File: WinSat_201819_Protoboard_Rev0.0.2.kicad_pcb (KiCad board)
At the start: 4 copper layers, 35.5 x 57.5 mm, 73 parts, among them J1 Conn_01x02_Female, J10 Conn_01x06_Male, J2 Conn_01x02_Female, J3 Conn_01x02_Female, J4 Conn_01x02_Female, J5 Conn_01x03_Female, J6 Conn_01x02_Female, J7 JTAG-6PIN, J8 Conn_01x03_Female, J9 Conn_01x03_Female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

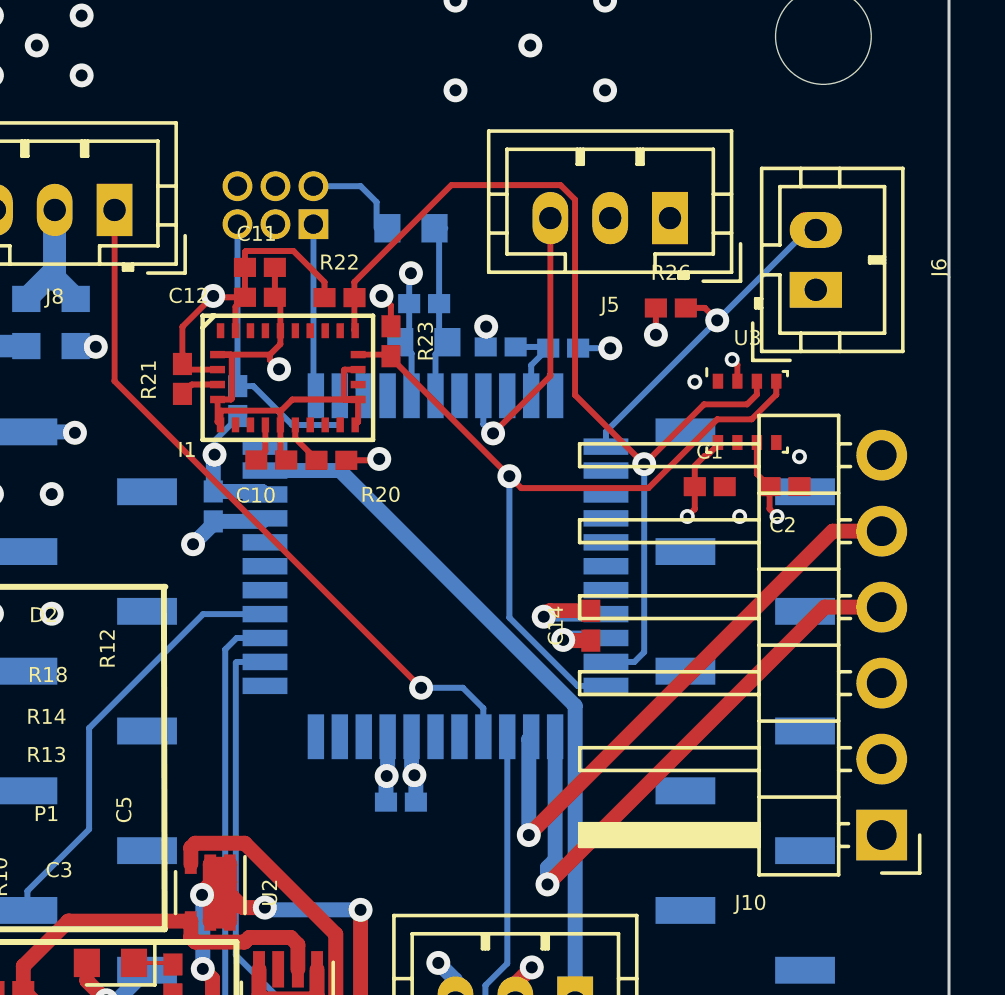
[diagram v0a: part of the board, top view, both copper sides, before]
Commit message: Cleaned up a few traces, fixed shoddy decoupling
Also moved BMP180 away from openlog header
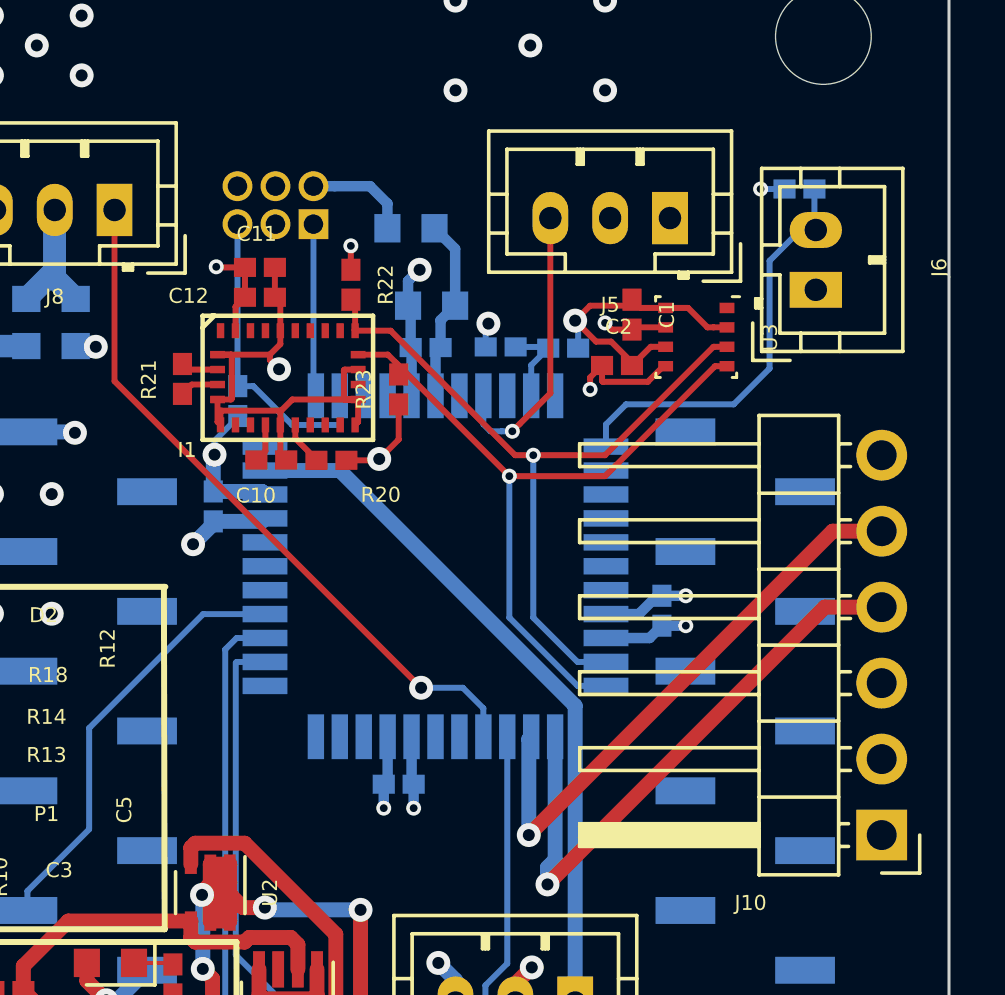
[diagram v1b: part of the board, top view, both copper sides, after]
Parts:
- C14, R26: moved to B.Cu
- moved C2 6.91 mm to (88.4, 85.7), turned to 180 degrees
- moved C1 6.31 mm to (88.9, 84.0), turned to 270 degrees
- moved R26 5.86 mm to (94.5, 79.8)
- moved U3 3.02 mm to (91.0, 84.8), turned to 270 degrees
- moved C14 2.43 mm to (89.9, 93.9)
- moved R23 1.63 mm to (81.1, 86.5), turned to 90 degrees
- moved C9 1.47 mm to (82.0, 85.1)
- moved C8 1.25 mm to (82.2, 83.7)
- moved C13 0.60 mm to (81.1, 99.7)
- moved R22 0.57 mm to (79.5, 83.0), turned to 270 degrees
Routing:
- net SDA1: track 33.2 -> 25.3 mm
- net GND: track 84.6 -> 90.1 mm, vias 39 -> 38
- net TEMP_SENSE-ADC: track 12.2 -> 14.0 mm, vias 1 -> 0
- net SCL1: track 26.5 -> 24.9 mm
- net +3V3: track 61.8 -> 60.6 mm, vias 21 -> 18

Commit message: Proto Final?
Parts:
- removed R17, R27: 1M, Resistor_SMD:R_0805_2012Metric
- added D4: DIODE, Diode_SMD:D_0603_1608Metric, B.Cu at (86.6, 120.9)
- added J11: USB_B_Micro, Connector_USB:USB_Micro-B_Molex-105017-0001, B.Cu at (86.4, 124.5)
- moved MK1 27.5 mm to (95.5, 124.0)
- moved MK3 27.4 mm to (68.1, 124.0)
- moved MK2 0.21 mm to (95.5, 74.7)
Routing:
- net +3V3: track 60.6 -> 51.9 mm
- net Net-(D4-Pad1): track 0.00 -> 2.21 mm
- net GND: track 90.1 -> 91.4 mm, vias 38 -> 63
- net BAT_POS: track 77.8 -> 78.7 mm, vias 2 -> 3
- net Net-(C8-Pad1): vias 0 -> 1
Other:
- board text added: "FTDI/ OPENLOG"
- board text added: "GPS"
- board text added: "HALL"
- board text added: "MOS0"
- board text added: "MOS1"
- board text added: "MOS2"
- board text added: "PDI"
- board text added: "SERVO"
- board text added: "THERM"

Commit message: Fixed Issues Thomas Saw
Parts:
- removed R18: 100k, OSD335x-KiCad-master:Not_Broken_0402
- added C16: 100nF, OSD335x-KiCad-master:Not_Broken_0402, F.Cu at (73.7, 84.6)
- J4: footprint Connector_PinHeader_2.54mm:PinHeader_1x02_P2.54mm_Vertical -> Connector_JST:JST_PH_B2B-PH-K_1x02_P2.00mm_Vertical
- R25: value 66K -> 7.15K
- moved R24 17.1 mm to (69.6, 86.6), turned to 180 degrees
- moved R25 13.3 mm to (71.4, 87.4), turned to 90 degrees
- moved R12 2.58 mm to (71.6, 108.0), turned to 0 degrees
- moved Q4 2.37 mm to (77.7, 122.9)
- moved D3 1.94 mm to (80.3, 123.4), turned to 270 degrees
- moved J4 1.94 mm to (73.7, 118.9), turned to 270 degrees
- moved D2 1.01 mm to (72.1, 106.4), turned to 0 degrees
- moved R21 0.50 mm to (73.7, 86.6)
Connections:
- R24 pad 2: +3V3 -> BAT_POS
- U9 pad 15: SERVO_TCL -> Net-(U9-Pad15)
- U9 pad 16: Net-(U9-Pad16) -> GPS_TX-MCU_RX
- U9 pad 29: Net-(U9-Pad29) -> SERVO_TCL
- U9 pad 32: GPS_TX-MCU_RX -> Net-(U9-Pad32)
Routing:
- net VOLTDIV_ADC: track 2.93 -> 19.3 mm, vias 0 -> 2
- net GPS_TX-MCU_RX: track 23.5 -> 10.6 mm, vias 0 -> 1
- net SERVO_TCL: track 23.5 -> 14.0 mm
- net GND: track 91.4 -> 99.6 mm, vias 63 -> 69
- net Net-(P1-Pad7): track 4.05 -> 0.00 mm
- net Net-(J4-Pad1): track 1.84 -> 4.38 mm
- net FTDI_OLOG_TX-MCU_RX: track 20.1 -> 17.6 mm
- net +3V3: track 51.9 -> 53.6 mm, vias 18 -> 19
- net FTDI_OLOG_RX-MCU_TX: track 19.3 -> 18.0 mm
- net REG_OUT: track 14.6 -> 13.4 mm
- net Net-(D3-Pad1): track 2.74 -> 3.43 mm
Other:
- board text added: "POW"

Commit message: Not sure what updated.
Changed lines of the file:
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@@
     (tags resistor)
     (attr smd)
-    (fp_text reference R12 (at -10.6194 2.6332) (layer F.SilkS)
+    (fp_text reference R12 (at -2.286 -11.43) (layer F.SilkS)
       (effects (font (size 0.5 0.5) (thickness 0.08)))
     )
@@
     (tags diode)
     (attr smd)
-    (fp_text reference D2 (at 2.0697 10.7298) (layer F.SilkS)
-      (effects (font (size 0.5 0.5) (thickness 0.08)))
-    )
+    (fp_text reference D2 (at -2.286 -10.922) (layer F.SilkS)
+      (effects (font (size 0.5 0.5) (thickness 0.08)))
+    )

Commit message: Change Board Size
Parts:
- added MK4: Mounting_Hole, MountingHole:MountingHole_3.2mm_M3, F.Cu at (57.2, 73.4)
- R29: value 0.025 OHM -> 0.05 OHM
- moved MK3 10.9 mm to (57.2, 124.3)
- moved MK2 1.34 mm to (95.3, 73.4)
- moved MK1 0.36 mm to (95.2, 124.2)
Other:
- board size 35.5 x 57.5 mm -> 46.7 x 59.5 mm
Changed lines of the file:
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@@
   (general
     (thickness 1.6)
-    (drawings 23)
+    (drawings 27)
     (tracks 616)
     (zones 0)
-    (modules 73)
+    (modules 74)
     (nets 102)
   )
@@
   (layers
     (0 F.Cu mixed)
-    (1 In1.Cu power)
-    (2 In2.Cu power)
+    (1 In1.Cu power hide)
+    (2 In2.Cu power hide)
     (31 B.Cu jumper)
     (36 B.SilkS user)
     (37 F.SilkS user)
-    (38 B.Mask user)
+    (38 B.Mask user hide)
     (39 F.Mask user)
     (44 Edge.Cuts user)
-    (45 Margin user)
+    (45 Margin user hide)
     (46 B.CrtYd user)
     (47 F.CrtYd user)
@@
     (add_net XBEE_TX-MCU_RX)
   )
+  (module MountingHole:MountingHole_3.2mm_M3 (layer F.Cu)
+    (at 57.2262 73.406)
+    (descr "Mounting Hole 3.2mm, no annular, M3")
+    (tags "mounting hole 3.2mm no annular m3")
+    (attr virtual)
+    (fp_text reference MK4 (at 0 -4.2) (layer F.SilkS) hide
+      (effects (font (size 1 1) (thickness 0.15)))
+    )
+    (fp_text value Mounting_Hole (at 0 4.2) (layer F.Fab)
+      (effects (font (size 1 1) (thickness 0.15)))
+    )
+    (fp_text user %R (at 0.3 0) (layer F.Fab)
+      (effects (font (size 1 1) (thickness 0.15)))
+    )
+    (fp_circle (center 0 0) (end 3.2 0) (layer Cmts.User) (width 0.15))
+    (fp_circle (center 0 0) (end 3.45 0) (layer F.CrtYd) (width 0.05))
+    (pad 1 np_thru_hole circle (at 0 0) (size 3.2 3.2) (drill 3.2) (layers *.Cu *.Mask))
+  )
   (module OSD335x-KiCad-master:Not_Broken_0402 (layer F.Cu)
     (at 73.66 84.582 270)
@@
   )
   (module MountingHole:MountingHole_3.2mm_M3 (layer F.Cu)
-    (at 95.504 123.952)
+    (at 95.25 124.206)
     (descr "Mounting Hole 3.2mm, no annular, M3")
     (tags "mounting hole 3.2mm no annular m3")
@@
   )
   (module MountingHole:MountingHole_3.2mm_M3 (layer F.Cu)
-    (at 95.504 74.676)
+    (at 95.3008 73.3552)
     (descr "Mounting Hole 3.2mm, no annular, M3")
     (tags "mounting hole 3.2mm no annular m3")
@@
   )
   (module MountingHole:MountingHole_3.2mm_M3 (layer F.Cu)
-    (at 68.072 123.952)
+    (at 57.2262 124.2568)
     (descr "Mounting Hole 3.2mm, no annular, M3")
     (tags "mounting hole 3.2mm no annular m3")
@@
       (effects (font (size 0.5 0.5) (thickness 0.08)))
     )
-    (fp_text value "0.025 OHM" (at 0 1.43 90) (layer F.Fab)
+    (fp_text value "0.05 OHM" (at 0 1.43 90) (layer F.Fab)
       (effects (font (size 1 1) (thickness 0.15)))
     )
@@
     )
   )
+  (gr_line (start 95.2754 69.1642) (end 57.277 69.088) (layer Edge.Cuts) (width 0.1))
+  (gr_line (start 99.6188 124.2568) (end 99.6442 73.533) (layer Edge.Cuts) (width 0.1))
+  (gr_line (start 57.3024 128.6256) (end 95.25 128.6256) (layer Edge.Cuts) (width 0.1))
+  (gr_line (start 52.9082 73.4568) (end 52.9844 124.3076) (layer Edge.Cuts) (width 0.1))
+  (gr_arc (start 95.2754 73.533) (end 99.6442 73.533) (angle -90) (layer Edge.Cuts) (width 0.1))
+  (gr_arc (start 95.25 124.2568) (end 95.25 128.6256) (angle -90) (layer Edge.Cuts) (width 0.1))
+  (gr_arc (start 57.3024 124.3076) (end 52.9844 124.3076) (angle -90) (layer Edge.Cuts) (width 0.1))
+  (gr_arc (start 57.277 73.4568) (end 57.277 69.088) (angle -90) (layer Edge.Cuts) (width 0.1))
   (gr_text POW (at 73.152 124.46) (layer F.SilkS)
     (effects (font (size 1.5 1.5) (thickness 0.3)))
@@
     (effects (font (size 1 1) (thickness 0.25)))
   )
-  (gr_line (start 99.5 70.5) (end 64 70.5) (layer Edge.Cuts) (width 0.1))
-  (gr_line (start 99.5 128) (end 99.5 70.5) (layer Edge.Cuts) (width 0.1))
-  (gr_line (start 64 128) (end 99.5 128) (layer Edge.Cuts) (width 0.1))
-  (gr_line (start 64 70.5) (end 64 128) (layer Edge.Cuts) (width 0.1))
   (gr_line (start 75.7 116.125) (end 73.05 116.125) (layer F.SilkS) (width 0.2))
   (gr_line (start 75.675 104.975) (end 75.7 116.125) (layer F.SilkS) (width 0.2))
@@
     (polygon
       (pts
-        (xy 65 127) (xy 103.825 127.175) (xy 104 67) (xy 65.175 66.825)
+        (xy 48.6946 127.0278) (xy 103.825 127.175) (xy 104 67) (xy 48.8696 66.8528)
       )
     )
@@
     (polygon
       (pts
-        (xy 65 127) (xy 103.5 127) (xy 103.5 67) (xy 65 67)
+        (xy 48.768 126.9036) (xy 103.5 127) (xy 103.5 67) (xy 48.768 66.9036)
       )
     )
@@
     (polygon
       (pts
-        (xy 65 67) (xy 65 117) (xy 103.825 117) (xy 103.825 67)
+        (xy 47.0408 66.8528) (xy 48.1076 117.8052) (xy 103.825 117) (xy 103.825 67)
       )
     )
@@
     (polygon
       (pts
-        (xy 65 67) (xy 65 127) (xy 103.5 127) (xy 103.5 67)
+        (xy 48.26 67.056) (xy 48.26 127.056) (xy 103.5 127) (xy 103.5 67)
       )
     )

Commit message: Make sure updated
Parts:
- removed Q3: SSM3K329R, Package_TO_SOT_SMD:SOT-23
- removed R15, R16: R_Small, Resistor_SMD:R_0603_1608Metric
- removed R3, R6: 0 OHM, Resistor_SMD:R_0603_1608Metric
- removed R9: 100K, OSD335x-KiCad-master:Not_Broken_0402
- added J12: Conn_01x03_Female, Connector_JST:JST_PH_S3B-PH-K_1x03_P2.00mm_Horizontal, F.Cu at (62.0, 86.9)
- J1, J2, J4, J6: footprint Connector_JST:JST_PH_B2B-PH-K_1x02_P2.00mm_Vertical -> Connector_JST:JST_PH_S2B-PH-K_1x02_P2.00mm_Horizontal
- J3: value Conn_01x02_Female -> Conn_01x03_Female; footprint Connector_JST:JST_PH_B2B-PH-K_1x02_P2.00mm_Vertical -> Connector_JST:JST_PH_S3B-PH-K_1x03_P2.00mm_Horizontal
- J5, J8, J9: footprint Connector_JST:JST_PH_B3B-PH-K_1x03_P2.00mm_Vertical -> Connector_JST:JST_PH_S3B-PH-K_1x03_P2.00mm_Horizontal
- moved J6 33.2 mm to (62.0, 79.8), turned to 270 degrees
- moved J9 32.3 mm to (71.9, 78.5)
- moved R26 30.4 mm to (64.3, 83.1), turned to 90 degrees
- moved J8 26.5 mm to (62.0, 105.2), turned to 270 degrees
- moved R4 25.0 mm to (71.4, 119.1), turned to 90 degrees
- moved J3 24.8 mm to (62.0, 96.0), turned to 270 degrees
- moved J1 23.7 mm to (73.1, 122.8), turned to 0 degrees
- moved R1 21.9 mm to (72.9, 119.0), turned to 90 degrees
- moved J11 20.9 mm to (65.5, 125.5)
- moved J10 18.7 mm to (85.3, 115.8), turned to 90 degrees
- moved Q1 16.5 mm to (75.6, 118.9), turned to 270 degrees
- moved R7 16.4 mm to (75.7, 116.6), turned to 180 degrees
- moved D4 16.4 mm to (70.6, 124.7), turned to 270 degrees
- moved J4 12.5 mm to (62.0, 114.6)
- moved Q4 12.3 mm to (66.0, 119.4)
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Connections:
- net SERVO_TCL renamed SERVO_TCL_1
- J3 pad 1: Net-(J3-Pad1) -> SERVO_TCL_2
- J3 pad 2: Net-(J3-Pad2) -> BAT_POS
- J8 pad 2: Net-(J8-Pad2) -> BAT_POS
- U9 pad 32: Net-(U9-Pad32) -> SERVO_TCL_2
- U9 pad 33: Net-(U9-Pad33) -> SERVO_TCL_3
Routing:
- net MOSFET2_GPIO: track 26.2 -> 0.00 mm, vias 1 -> 0
- net SERVO_TCL_2: track 0.00 -> 21.4 mm, vias 0 -> 1
- net TEMP_SENSE-ADC: track 14.0 -> 34.7 mm, vias 0 -> 2
- net GPS_TX-MCU_RX: track 10.6 -> 30.3 mm, vias 1 -> 2
- net SERVO_TCL_3: track 0.00 -> 15.5 mm, vias 0 -> 1
- net GND: track 99.6 -> 111.8 mm, vias 69 -> 49
- net +3V3: track 53.6 -> 44.3 mm, vias 19 -> 18
- net FTDI_OLOG_RX-MCU_TX: track 18.0 -> 25.2 mm, vias 1 -> 0
- net Net-(J8-Pad2): track 6.63 -> 0.00 mm
- net SERVO_TCL_1: track 14.0 -> 20.5 mm
- net BAT_POS: track 78.8 -> 84.5 mm
- net VOLTDIV_ADC: track 19.3 -> 24.7 mm
- net Net-(J3-Pad1): track 4.72 -> 0.00 mm
- net Net-(D4-Pad1): track 2.21 -> 5.56 mm
- net Net-(J3-Pad2): track 3.19 -> 0.00 mm
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- added copper zone on B.Cu, net BAT_POS
- removed copper zone on F.Cu, net BAT_POS
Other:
- board text added: "POWER"
- board text added: "SERVO 1"
- board text added: "SERVO 2"
- board text added: "SERVO 3"
- board text added: "TEMP"
- board text removed: "MOS0"
- board text removed: "SERVO"
- board text removed: "THERM"

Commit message: Bye Overcurrent
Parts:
- removed R29: 0.05 OHM, Resistor_SMD:R_0603_1608Metric
- removed U1: LTC4361, Package_TO_SOT_SMD:TSOT-23-8
- removed U2: Si1470DH, Package_TO_SOT_SMD:SOT-363_SC-70-6
- C13, C14, C15: value C_Small -> 100nF
- C6: value 10 uF -> 10uF
- D1: value LED -> LED Red
- D2: value LED -> LED Blue
- L1: value 10uH -> 22uH
- moved R12 0.36 mm to (71.9, 107.7)
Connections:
- C5 pad 1: REG_OUT -> Net-(C15-Pad1)
- P1 pad 4: REG_OUT -> Net-(C15-Pad1)
- P1 pad 5: REG_OUT -> Net-(C15-Pad1)
- R14 pad 2: REG_OUT -> Net-(C15-Pad1)
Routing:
- net Net-(R29-Pad2): track 28.4 -> 0.00 mm, vias 4 -> 0
- net REG_OUT: track 13.4 -> 0.00 mm
- net Net-(U1-Pad7): track 11.4 -> 0.00 mm
- net GND: track 111.8 -> 107.4 mm, vias 49 -> 48
- net Net-(C15-Pad1): track 15.4 -> 16.7 mm
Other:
- board text added: "CANSAT ASTROTRAIN #2591"
- board text added: "JARES DOVERSPIKE JRD0027@UAH.EDU"
- board text added: "NO U"
- board text added: "VERSION 1.0A"
- board text removed: "POW"
